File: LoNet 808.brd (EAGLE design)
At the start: 46.5 x 27.7 mm, 25 parts, among them CN2 JST-2.0, J4 MICRO-SMD, U1 TXB0104PWR

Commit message: add components
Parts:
- added C5: 470uf, Seeed-OPL-Capacitor:AVX-D
- added C6: 220uf, Seeed-OPL-Capacitor:AVX-E
- added D6: 28V-5A, Seeed-OPL-Diode:DO-214AA
- added IC1: LM2596S, national-semiconductor:TO263-5
- added J5: DC-005, Seeed-OPL-Connector:DCJ3P-14.2X11.0X9.0MM
- added L2: 22UH, Seeed-OPL-Inductor:SMD-2P-2.0X1.2X1.0MM
- added U2: (no value), LBRmicrobuilder:SOT23-5
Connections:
- new net VDD: U2.4
- new net VSS: U2.2
- net GND: now also IC1.3
- net VBAT: now also U2.3

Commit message: add components
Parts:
- removed C5: 470uf, Seeed-OPL-Capacitor:AVX-D
- removed C6: 220uf, Seeed-OPL-Capacitor:AVX-E
- added CT1: 100UF, Seeed-OPL-Capacitor:ELECTRO-SMD-C-6MM
- added CT2: 220UF, Seeed-OPL-Capacitor:ELECTRO-SMD-C-6MM
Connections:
- new net N$1: CT1.+, IC1.1, J5.+
- new net N$2: D6.-, IC1.2, L2.1
- new net N$3: CT1.-, IC1.3, IC1.5, J5.-1, J5.-2
- new net N$5: CT2.-, D6.+
- new net N$7: CT2.+, IC1.4, L2.2
- net GND: no longer IC1.3
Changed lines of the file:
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@@
 <attribute name="MPN" value="MPH201210S22RMT" x="-14.224" y="-24.638" size="1.778" layer="27" display="off"/>
 </element>
-<element name="C5" library="Seeed-OPL-Capacitor" package="AVX-D" value="470uf" x="-11.938" y="-30.48"/>
-<element name="C6" library="Seeed-OPL-Capacitor" package="AVX-E" value="220uf" x="-11.938" y="-38.1">
-<attribute name="MPN" value="TAJE227K016RNJ" x="-11.938" y="-38.1" size="1.778" layer="27" display="off"/>
+<element name="CT1" library="Seeed-OPL-Capacitor" package="ELECTRO-SMD-C-6MM" value="100UF" x="-20.955" y="-36.957">
+<attribute name="MPN" value="CS1H101M-CRE77" x="-20.955" y="-36.957" size="1.778" layer="27" display="off"/>
+</element>
+<element name="CT2" library="Seeed-OPL-Capacitor" package="ELECTRO-SMD-C-6MM" value="220UF" x="-29.464" y="-36.957">
+<attribute name="MPN" value="CS1E221M-CRE77" x="-29.464" y="-36.957" size="1.778" layer="27" display="off"/>
 </element>
 </elements>
@@
 <wire x1="30.226" y1="22.225" x2="33.655" y2="22.225" width="0.2032" layer="16"/>
 <wire x1="33.655" y1="22.225" x2="33.909" y2="21.971" width="0.2032" layer="16"/>
-<contactref element="IC1" pad="3"/>
 <wire x1="41.7322" y1="23.8506" x2="43.561" y2="23.495" width="0" layer="19" extent="1-1"/>
 <wire x1="40.8432" y1="23.3426" x2="41.7322" y2="23.8506" width="0" layer="19" extent="1-1"/>
@@
 <wire x1="30.3784" y1="3.9624" x2="30.702" y2="1.97" width="0" layer="19" extent="1-1"/>
 <wire x1="29.3624" y1="3.9624" x2="30.3784" y2="3.9624" width="0" layer="19" extent="1-1"/>
-<wire x1="-9.398" y1="-14.8082" x2="3.048" y2="3.683" width="0" layer="19" extent="1-1"/>
 </signal>
 <signal name="VBUS">
@@
 <contactref element="U2" pad="2"/>
 </signal>
+<signal name="N$1">
+<contactref element="J5" pad="+"/>
+<contactref element="IC1" pad="1"/>
+<contactref element="CT1" pad="+"/>
+<wire x1="-12.8016" y1="-14.8082" x2="-18.288" y2="-36.957" width="0" layer="19" extent="1-1"/>
+<wire x1="12.192" y1="-10.033" x2="-12.8016" y2="-14.8082" width="0" layer="19" extent="1-1"/>
+</signal>
+<signal name="N$3">
+<contactref element="IC1" pad="5"/>
+<contactref element="IC1" pad="3"/>
+<contactref element="J5" pad="-2"/>
+<contactref element="J5" pad="-1"/>
+<contactref element="CT1" pad="-"/>
+<wire x1="-9.398" y1="-14.8082" x2="-23.622" y2="-36.957" width="0" layer="19" extent="1-1"/>
+<wire x1="-5.9944" y1="-14.8082" x2="-9.398" y2="-14.8082" width="0" layer="19" extent="1-1"/>
+<wire x1="5.969" y1="-10.033" x2="-5.9944" y2="-14.8082" width="0" layer="19" extent="1-1"/>
+<wire x1="9.017" y1="-14.986" x2="5.969" y2="-10.033" width="0" layer="19" extent="1-1"/>
+</signal>
+<signal name="N$2">
+<contactref element="IC1" pad="2"/>
+<contactref element="L2" pad="1"/>
+<contactref element="D6" pad="-"/>
+<wire x1="-10.998" y1="-19.304" x2="-15.024" y2="-24.638" width="0" layer="19" extent="1-1"/>
+<wire x1="-11.0998" y1="-14.8082" x2="-10.998" y2="-19.304" width="0" layer="19" extent="1-1"/>
+</signal>
+<signal name="N$7">
+<contactref element="L2" pad="2"/>
+<contactref element="CT2" pad="+"/>
+<contactref element="IC1" pad="4"/>
+<wire x1="-13.424" y1="-24.638" x2="-26.797" y2="-36.957" width="0" layer="19" extent="1-1"/>
+<wire x1="-7.6962" y1="-14.8082" x2="-13.424" y2="-24.638" width="0" layer="19" extent="1-1"/>
+</signal>
+<signal name="N$5">
+<contactref element="CT2" pad="-"/>
+<contactref element="D6" pad="+"/>
+<wire x1="-15.418" y1="-19.304" x2="-32.131" y2="-36.957" width="0" layer="19" extent="1-1"/>
+</signal>
 </signals>

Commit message: add more
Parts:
- added C5: 10uf, Seeed-OPL-Capacitor:C0603
- added D7: YELLOW-0603, Seeed-OPL-Diode:LED-0603
- added D9: GREEN-0603, Seeed-OPL-Diode:LED-0603
- added R1: 1K, Seeed-OPL-Resistor:R0603
- added R2: 470R, Seeed-OPL-Resistor:R0603
- added R3: 2K, Seeed-OPL-Resistor:R0603
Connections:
- removed net N$3: CT1.-, IC1.3, IC1.5, J5.-1, J5.-2
- removed net VDD: U2.4
- removed net VSS: U2.2
- new net N$11: R1.2, R2.2, U2.1
- new net N$12: D9.+, R1.1
- new net N$13: D7.-, R2.1
- new net N$14: R3.1, U2.5
- net GND: now also CT1.-, IC1.3, IC1.5, J5.-1, J5.-2
- net N$5: now also C5.1, D9.-, R3.2, U2.2
- net N$7: now also C5.2, D7.+, U2.4
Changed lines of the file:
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@@
 <attribute name="MPN" value="CS1E221M-CRE77" x="-29.464" y="-36.957" size="1.778" layer="27" display="off"/>
+</element>
+<element name="C5" library="Seeed-OPL-Capacitor" package="C0603" value="10uf" x="-35.814" y="-38.227">
+<attribute name="MPN" value="CC0603KRX5R6BB106" x="-35.814" y="-38.227" size="1.778" layer="27" display="off"/>
+</element>
+<element name="D7" library="Seeed-OPL-Diode" package="LED-0603" value="YELLOW-0603" x="-35.433" y="-43.942">
+<attribute name="MPN" value="19-217-Y5C-AM1N1VY-3T" x="-35.433" y="-43.942" size="1.778" layer="27" display="off"/>
+</element>
+<element name="D9" library="Seeed-OPL-Diode" package="LED-0603" value="GREEN-0603" x="-35.433" y="-48.133">
+<attribute name="MPN" value="19-217-G7C-AN1P2-3T" x="-35.433" y="-48.133" size="1.778" layer="27" display="off"/>
+</element>
+<element name="R1" library="Seeed-OPL-Resistor" package="R0603" value="1K" x="-40.386" y="-47.752">
+<attribute name="MPN" value="RC0603FR-071KL" x="-40.386" y="-47.752" size="1.778" layer="27" display="off"/>
+</element>
+<element name="R2" library="Seeed-OPL-Resistor" package="R0603" value="470R" x="-45.085" y="-47.752">
+<attribute name="MPN" value="RC0603JR-07470RL" x="-45.085" y="-47.752" size="1.778" layer="27" display="off"/>
+</element>
+<element name="R3" library="Seeed-OPL-Resistor" package="R0603" value="2K" x="-49.784" y="-47.752">
+<attribute name="MPN" value="RC0603FR-072KL" x="-49.784" y="-47.752" size="1.778" layer="27" display="off"/>
 </element>
 </elements>
@@
 <wire x1="30.226" y1="22.225" x2="33.655" y2="22.225" width="0.2032" layer="16"/>
 <wire x1="33.655" y1="22.225" x2="33.909" y2="21.971" width="0.2032" layer="16"/>
+<contactref element="IC1" pad="5"/>
+<contactref element="IC1" pad="3"/>
+<contactref element="J5" pad="-2"/>
+<contactref element="J5" pad="-1"/>
+<contactref element="CT1" pad="-"/>
 <wire x1="41.7322" y1="23.8506" x2="43.561" y2="23.495" width="0" layer="19" extent="1-1"/>
 <wire x1="40.8432" y1="23.3426" x2="41.7322" y2="23.8506" width="0" layer="19" extent="1-1"/>
@@
 <wire x1="30.3784" y1="3.9624" x2="30.702" y2="1.97" width="0" layer="19" extent="1-1"/>
 <wire x1="29.3624" y1="3.9624" x2="30.3784" y2="3.9624" width="0" layer="19" extent="1-1"/>
+<wire x1="5.969" y1="-10.033" x2="9.4996" y2="1.016" width="0" layer="19" extent="1-1"/>
+<wire x1="9.017" y1="-14.986" x2="5.969" y2="-10.033" width="0" layer="19" extent="1-1"/>
+<wire x1="-5.9944" y1="-14.8082" x2="5.969" y2="-10.033" width="0" layer="19" extent="1-1"/>
+<wire x1="-9.398" y1="-14.8082" x2="-5.9944" y2="-14.8082" width="0" layer="19" extent="1-1"/>
+<wire x1="-23.622" y1="-36.957" x2="-9.398" y2="-14.8082" width="0" layer="19" extent="1-1"/>
 </signal>
 <signal name="VBUS">
@@
 <wire x1="25.273" y1="20.955" x2="22.86" y2="18.542" width="0.2032" layer="1"/>
 </signal>
-<signal name="VDD">
-<contactref element="U2" pad="4"/>
-</signal>
-<signal name="VSS">
-<contactref element="U2" pad="2"/>
-</signal>
 <signal name="N$1">
 <contactref element="J5" pad="+"/>
@@
 <wire x1="12.192" y1="-10.033" x2="-12.8016" y2="-14.8082" width="0" layer="19" extent="1-1"/>
 </signal>
-<signal name="N$3">
-<contactref element="IC1" pad="5"/>
-<contactref element="IC1" pad="3"/>
-<contactref element="J5" pad="-2"/>
-<contactref element="J5" pad="-1"/>
-<contactref element="CT1" pad="-"/>
-<wire x1="-9.398" y1="-14.8082" x2="-23.622" y2="-36.957" width="0" layer="19" extent="1-1"/>
-<wire x1="-5.9944" y1="-14.8082" x2="-9.398" y2="-14.8082" width="0" layer="19" extent="1-1"/>
-<wire x1="5.969" y1="-10.033" x2="-5.9944" y2="-14.8082" width="0" layer="19" extent="1-1"/>
-<wire x1="9.017" y1="-14.986" x2="5.969" y2="-10.033" width="0" layer="19" extent="1-1"/>
-</signal>
 <signal name="N$2">
 <contactref element="IC1" pad="2"/>
@@
 <contactref element="CT2" pad="+"/>
 <contactref element="IC1" pad="4"/>
+<contactref element="C5" pad="2"/>
+<contactref element="U2" pad="4"/>
+<contactref element="D7" pad="+"/>
+<wire x1="-35.814" y1="-38.989" x2="-36.195" y2="-43.942" width="0" layer="19" extent="1-1"/>
+<wire x1="-26.797" y1="-36.957" x2="-35.814" y2="-38.989" width="0" layer="19" extent="1-1"/>
 <wire x1="-13.424" y1="-24.638" x2="-26.797" y2="-36.957" width="0" layer="19" extent="1-1"/>
 <wire x1="-7.6962" y1="-14.8082" x2="-13.424" y2="-24.638" width="0" layer="19" extent="1-1"/>
+<wire x1="0.823" y1="-1.7479" x2="-7.6962" y2="-14.8082" width="0" layer="19" extent="1-1"/>
 </signal>
 <signal name="N$5">
 <contactref element="CT2" pad="-"/>
 <contactref element="D6" pad="+"/>
+<contactref element="C5" pad="1"/>
+<contactref element="D9" pad="-"/>
+<contactref element="R3" pad="2"/>
+<contactref element="U2" pad="2"/>
+<wire x1="-34.671" y1="-48.133" x2="-49.784" y2="-48.514" width="0" layer="19" extent="1-1"/>
+<wire x1="-35.814" y1="-37.465" x2="-34.671" y2="-48.133" width="0" layer="19" extent="1-1"/>
+<wire x1="-32.131" y1="-36.957" x2="-35.814" y2="-37.465" width="0" layer="19" extent="1-1"/>
 <wire x1="-15.418" y1="-19.304" x2="-32.131" y2="-36.957" width="0" layer="19" extent="1-1"/>
+<wire x1="-0.127" y1="-4.3481" x2="-15.418" y2="-19.304" width="0" layer="19" extent="1-1"/>
+</signal>
+<signal name="N$11">
+<contactref element="U2" pad="1"/>
+<contactref element="R2" pad="2"/>
+<contactref element="R1" pad="2"/>
+<wire x1="-40.386" y1="-48.514" x2="-45.085" y2="-48.514" width="0" layer="19" extent="1-1"/>
+<wire x1="-1.077" y1="-4.3481" x2="-40.386" y2="-48.514" width="0" layer="19" extent="1-1"/>
+</signal>
+<signal name="N$12">
+<contactref element="D9" pad="+"/>
+<contactref element="R1" pad="1"/>
+<wire x1="-36.195" y1="-48.133" x2="-40.386" y2="-46.99" width="0" layer="19" extent="1-1"/>
+</signal>
+<signal name="N$13">
+<contactref element="D7" pad="-"/>
+<contactref element="R2" pad="1"/>
+<wire x1="-34.671" y1="-43.942" x2="-45.085" y2="-46.99" width="0" layer="19" extent="1-1"/>
+</signal>
+<signal name="N$14">
+<contactref element="U2" pad="5"/>
+<contactref element="R3" pad="1"/>
+<wire x1="-1.077" y1="-1.7479" x2="-49.784" y2="-46.99" width="0" layer="19" extent="1-1"/>
 </signal>
 </signals>

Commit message: add mcu
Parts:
- added U3: ATMEGA328P-AU-TQFP32, Seeed-OPL-ic:TQFP32-0.8-7X7MM
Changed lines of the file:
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@@
 <attribute name="MPN" value="RC0603FR-072KL" x="-49.784" y="-47.752" size="1.778" layer="27" display="off"/>
+</element>
+<element name="U3" library="Seeed-OPL-ic" package="TQFP32-0.8-7X7MM" value="ATMEGA328P-AU-TQFP32" x="-57.023" y="-45.212">
+<attribute name="MPN" value="ATMEGA328P-AU" x="-57.023" y="-45.212" size="1.778" layer="27" display="off"/>
 </element>
 </elements>

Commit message: more connection
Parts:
- added C6: 100nf, Seeed-OPL-Capacitor:C0603
- added D10: BLUE-0603, Seeed-OPL-Diode:LED-0603
- added R5: 1.5K, Seeed-OPL-Resistor:R0603
- added R6: 10K, Seeed-OPL-Resistor:R0603
- added U$23: RESONATORSMD, SparkFun:RESONATOR-SMD
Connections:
- removed net N$5 (its old number): C5.1, CT2.-, D6.+, D9.-, R3.2, U2.2
- new net N$11: C6.2, U3.20
- new net N$13: R5.1, U3.13
- new net N$14: D10.+, R5.2
- new net N$15: U$23.1, U3.7
- new net N$16: U$23.3, U3.8
- new net RST: R6.2, U3.29
- net GND: now also C5.1, C6.1, CT2.-, D10.-, D6.+, D9.-, R3.2, U$23.2, U2.2, U3.21, U3.3, U3.5
- net VBAT: now also R6.1, U3.18, U3.4, U3.6

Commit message: more connection
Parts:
- removed C3: 1uF, Common:0603
- removed J3: (no value), Connector:2P-2.54-65/35MIL
- removed J4: MICRO-SMD, Connector:MICRO-SMD
- added C7: 100nf, Seeed-OPL-Capacitor:C0603
- added JP1: (no value), SparkFun-Connectors:1X06
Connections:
- removed net H_VIO: J2.7, U1.14
- removed net N$7: C5.2, CT2.+, D7.+, IC1.4, L2.2, U2.4
- new net N$18: C7.1, JP1.6
- net GND: now also JP1.1; no longer C3.1, J3.1, J4.P5, J4.S1, J4.S2, J4.S3, J4.S4, J4.S5, J4.S6
- net H_RXD: now also JP1.5, U3.31
- net H_TXD: now also JP1.4, U3.30
- net RST: now also C7.2
- net VBAT: now also J2.7, U1.14
- net VBUS: now also C5.2, CT2.+, D7.+, IC1.4, JP1.3, L2.2, U2.4; no longer C3.2, J3.2, J4.P1, U$1.25
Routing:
- net VBAT: track 60.3 -> 108.7 mm, vias 1 -> 3
- net H_VIO: track 48.5 -> 0.00 mm, vias 2 -> 0
- net VBUS: track 32.5 -> 0.00 mm, vias 1 -> 0
- net GND: track 14.4 -> 11.3 mm

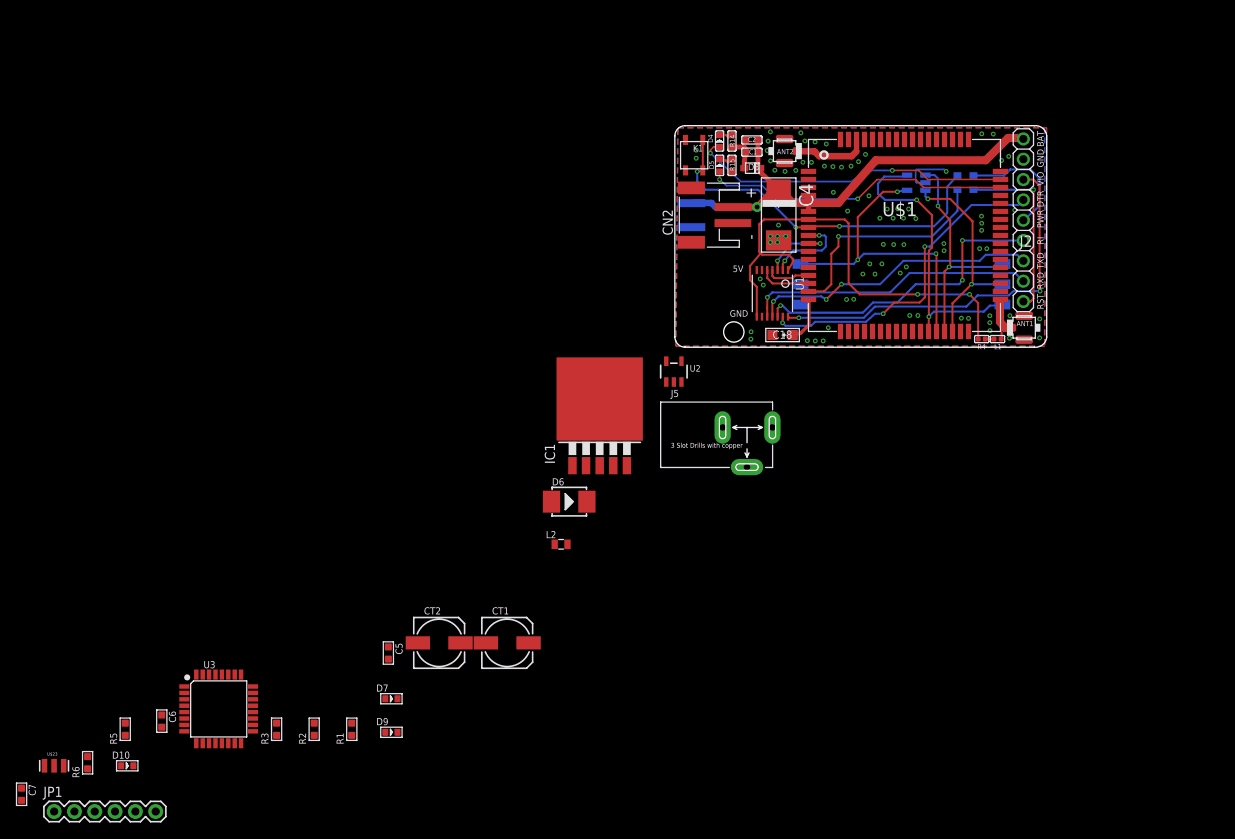
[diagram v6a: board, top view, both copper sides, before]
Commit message: add RFM83C
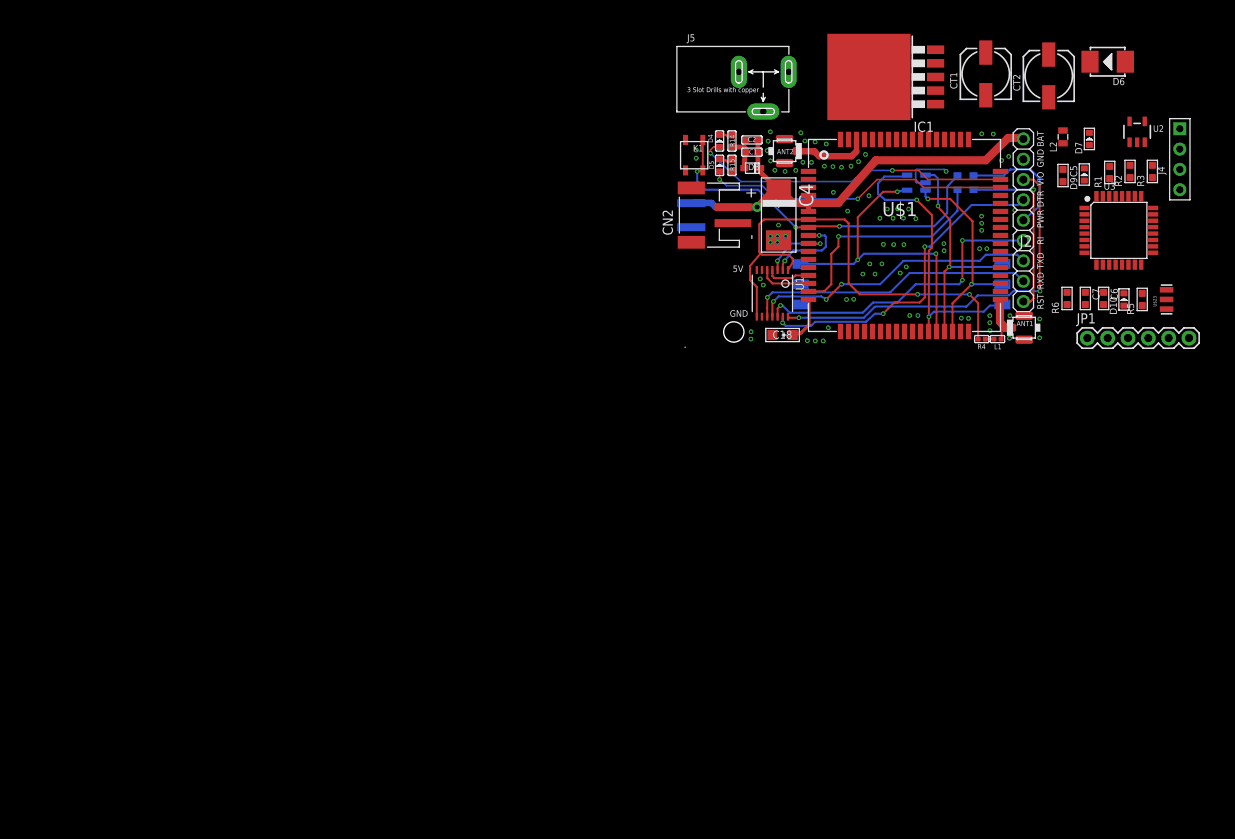
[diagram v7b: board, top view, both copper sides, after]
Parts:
- added J4: 4p-2.54, Seeed-OPL-Connector:H4-2.54
- moved U$23 150.8 mm to (61.5, 5.97), turned to 90 degrees
- moved C7 146.7 mm to (51.3, 6.10)
- moved JP1 142.1 mm to (51.6, 1.14)
- moved R5 138.0 mm to (58.4, 5.97)
- moved D10 137.5 mm to (56.1, 5.97), turned to 90 degrees
- moved R6 135.5 mm to (49.0, 6.10)
- moved R3 129.8 mm to (59.7, 22.0)
- moved C6 129.0 mm to (53.6, 6.10)
- moved U3 127.4 mm to (55.5, 14.6)
- moved R2 123.5 mm to (56.9, 22.0)
- moved R1 117.6 mm to (54.4, 21.8)
- moved D7 111.8 mm to (51.8, 26.0), turned to 90 degrees
- moved D9 111.2 mm to (51.2, 21.6), turned to 90 degrees
- moved CT2 104.1 mm to (46.7, 33.9), turned to 90 degrees
- moved C5 103.3 mm to (48.5, 21.5)
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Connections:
- new net D2: J4.2, U3.32
- net GND: now also J4.1
- net VBAT: now also J4.3
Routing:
- removed copper zone on layer 1, net GND
- removed copper zone on layer 16, net GND
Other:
- board size 46.5 x 27.7 mm -> 7 x 6.8 mm

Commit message: get berber files
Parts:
- moved J4 8.90 mm to (62.6, 32.4)
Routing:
- net GND: track 11.3 -> 380.5 mm
- net VBUS: track 0.00 -> 122.6 mm, vias 0 -> 1
- net VBAT: track 108.7 -> 188.0 mm
- net H_RXD: track 36.1 -> 72.0 mm, vias 1 -> 2
- net H_TXD: track 36.2 -> 71.7 mm, vias 3 -> 5
- net N$1: track 0.00 -> 32.9 mm
- net N$2: track 0.00 -> 28.9 mm, vias 0 -> 3
- net RST: track 0.00 -> 22.7 mm
- net D2: track 0.00 -> 19.9 mm, vias 0 -> 1
- net N$18: track 0.00 -> 17.0 mm, vias 0 -> 1
- net N$15: track 0.00 -> 15.9 mm, vias 0 -> 2
- net N$16: track 0.00 -> 13.0 mm
- net N$11: track 0.00 -> 12.1 mm, vias 0 -> 2
- net N$3: track 0.00 -> 7.63 mm
- net N$8: track 0.00 -> 6.87 mm
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- added copper zone on layer 1, net GND
- added copper zone on layer 16, net GND
